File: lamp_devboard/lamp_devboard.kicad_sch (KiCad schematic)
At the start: 18 parts, among them J101 Screw_Terminal_01x02, J102 Screw_Terminal_01x02, J103 Conn_01x02_Female, J104 Conn_01x02_Male, J105 Conn_01x02_Female, J106 Conn_01x02_Male, J107 Screw_Terminal_01x02, J108 Screw_Terminal_01x02

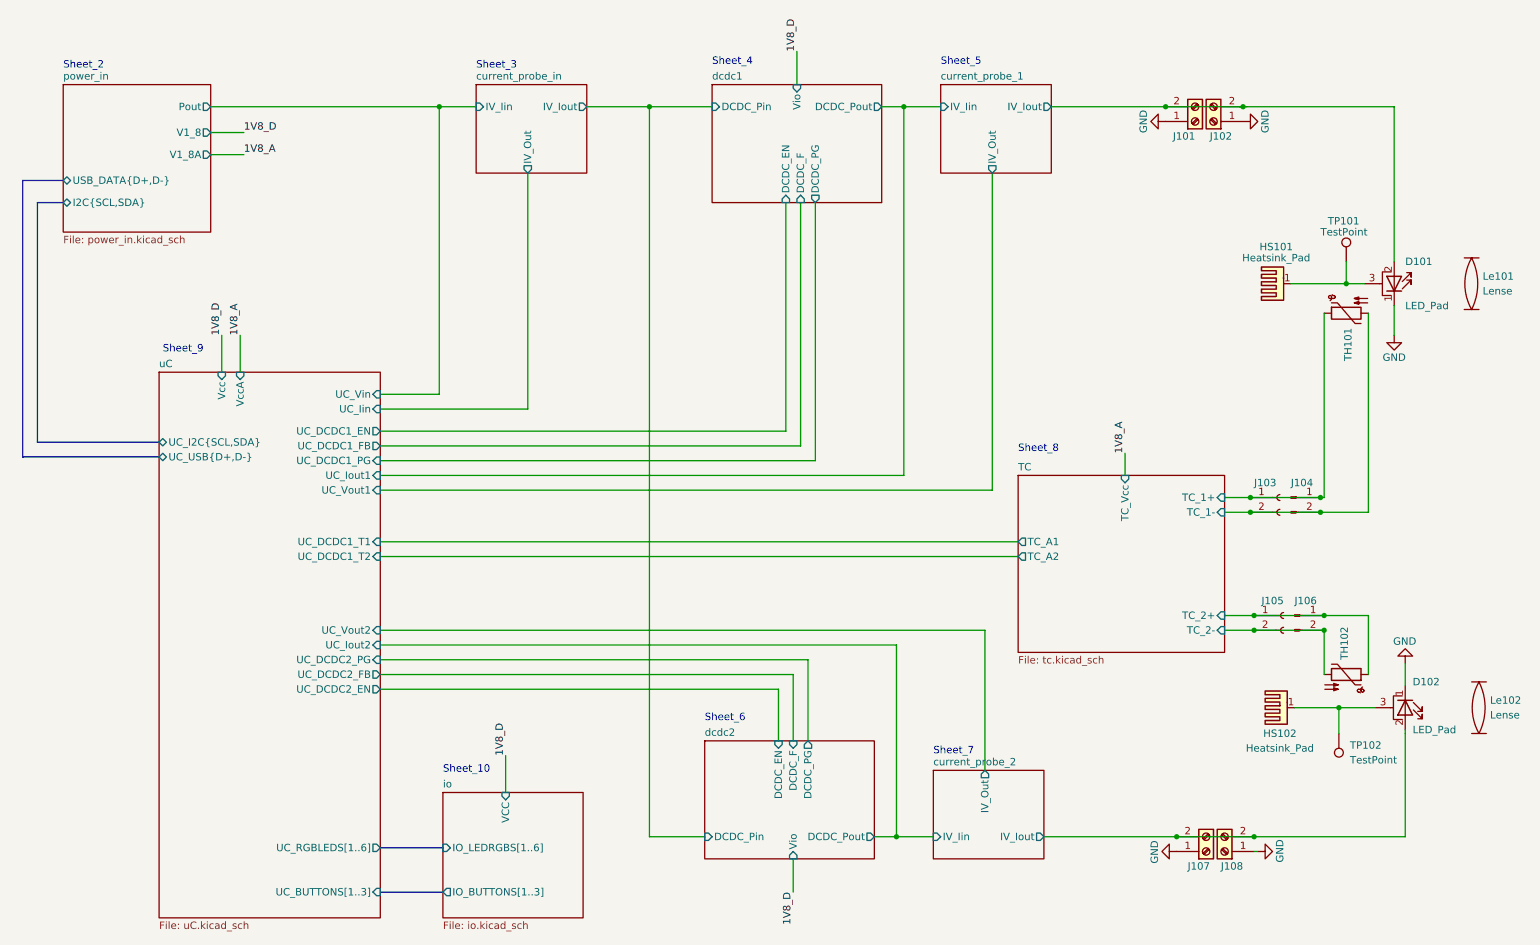
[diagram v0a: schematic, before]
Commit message: schematics, add battery to power module
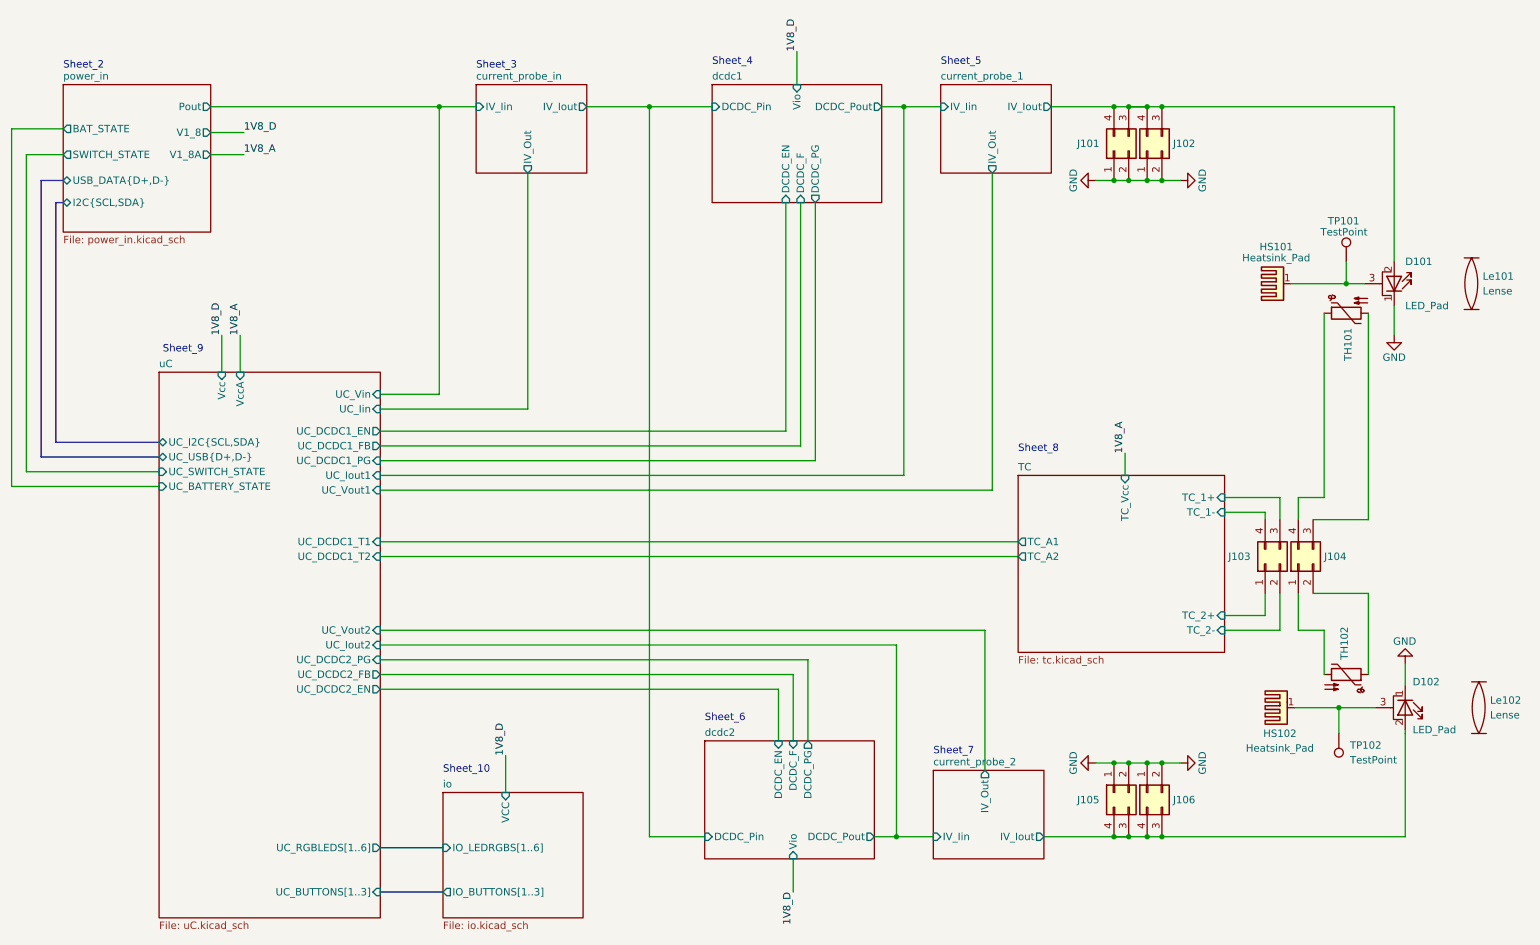
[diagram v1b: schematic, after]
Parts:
- removed J101, J107: Screw_Terminal_01x02, Connector_Phoenix_MC:PhoenixContact_MC_1,5_2-G-3.81_1x02_P3.81mm_Horizontal, symbol Connector:Screw_Terminal_01x02
- removed J102, J108: Screw_Terminal_01x02, Connector_Phoenix_MC:PhoenixContact_MCV_1,5_2-G-3.81_1x02_P3.81mm_Vertical, symbol Connector:Screw_Terminal_01x02
- removed J103, J105: Conn_01x02_Female, Connector_PinSocket_2.54mm:PinSocket_1x02_P2.54mm_Horizontal, symbol Connector:Conn_01x02_Female
- removed J104, J106: Conn_01x02_Male, Connector_PinHeader_2.54mm:PinHeader_1x02_P2.54mm_Vertical, symbol Connector:Conn_01x02_Male
- added J101, J103, J105: Conn_02x02_Counter_Clockwise, Connector_PinSocket_2.54mm:PinSocket_2x02_P2.54mm_Horizontal, symbol Connector_Generic:Conn_02x02_Counter_Clockwise
- added J102, J104, J106: Conn_02x02_Counter_Clockwise, Connector_PinHeader_2.54mm:PinHeader_2x02_P2.54mm_Vertical, symbol Connector_Generic:Conn_02x02_Counter_Clockwise
- TH101: footprint (none) -> Resistor_SMD:R_0805_2012Metric_Pad1.20x1.40mm_HandSolder
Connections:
- net GND: now also J101.1 (Pin_1), J101.2 (Pin_2), J102.1 (Pin_1), J102.2 (Pin_2), J105.1 (Pin_1), J105.2 (Pin_2), J106.1 (Pin_1), J106.2 (Pin_2)
- net TC/TC_1+: now also J103.3 (Pin_3); no longer TH101.1
- net TC/TC_1-: now also J103.4 (Pin_4); no longer TH101.2
- net TC/TC_2+: now also J103.1 (Pin_1); no longer TH102.1
- net TC/TC_2-: now also J103.2 (Pin_2); no longer TH102.2
- net current_probe_1/IV_Iout: now also J101.3 (Pin_3), J101.4 (Pin_4), J102.3 (Pin_3), J102.4 (Pin_4)
- net current_probe_2/IV_Iout: now also J105.3 (Pin_3), J105.4 (Pin_4), J106.3 (Pin_3), J106.4 (Pin_4)
- new net: J104.1 (Pin_1), TH102.2
- new net: J104.2 (Pin_2), TH102.1
- new net: J104.3 (Pin_3), TH101.2
- new net: J104.4 (Pin_4), TH101.1
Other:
- sheet power_in ports: added BAT_STATE, SWITCH_STATE; removed none
- sheet uC ports: added UC_BATTERY_STATE, UC_SWITCH_STATE; removed none

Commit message: some changes
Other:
- sheet io ports: added IO_BUTTONS[1..2], IO_LEDRGBS[1..3]; removed IO_BUTTONS[1..3], IO_LEDRGBS[1..6]
- sheet uC ports: added UC_BUTTONS[1..2], UC_RGBLEDS[1..3]; removed UC_BUTTONS[1..3], UC_RGBLEDS[1..6]

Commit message: first version of the pcb board
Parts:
- TP101, TP102: footprint (none) -> TestPoint:TestPoint_Pad_1.0x1.0mm
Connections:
- net GND: no longer D101.1 (K), D102.1 (K), J102.1 (Pin_1), J102.2 (Pin_2), J106.1 (Pin_1), J106.2 (Pin_2)
- net current_probe_1/IV_Iout: no longer D101.2 (A), J102.3 (Pin_3), J102.4 (Pin_4)
- net current_probe_2/IV_Iout: no longer D102.2 (A), J106.3 (Pin_3), J106.4 (Pin_4)
- new net GND1: D101.1 (K), J102.1 (Pin_1), J102.2 (Pin_2)
- new net GND2: D102.1 (K), J106.1 (Pin_1), J106.2 (Pin_2)
- new net LED1_Pin: D101.2 (A), J102.3 (Pin_3), J102.4 (Pin_4)
- new net LED2_Pin: D102.2 (A), J106.3 (Pin_3), J106.4 (Pin_4)
